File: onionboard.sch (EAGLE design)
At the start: 173 parts, among them IC1 IR4427S, IC2 IR4427S, J1 22-27-2041-04, Q1 FDD4141TO252, Q2 FDD4141TO252, Q3 FDD4141TO252, Q4 FDD4141TO252, Q5 FDD4141TO252, Q6 FDD4141TO252, X1 5569-8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

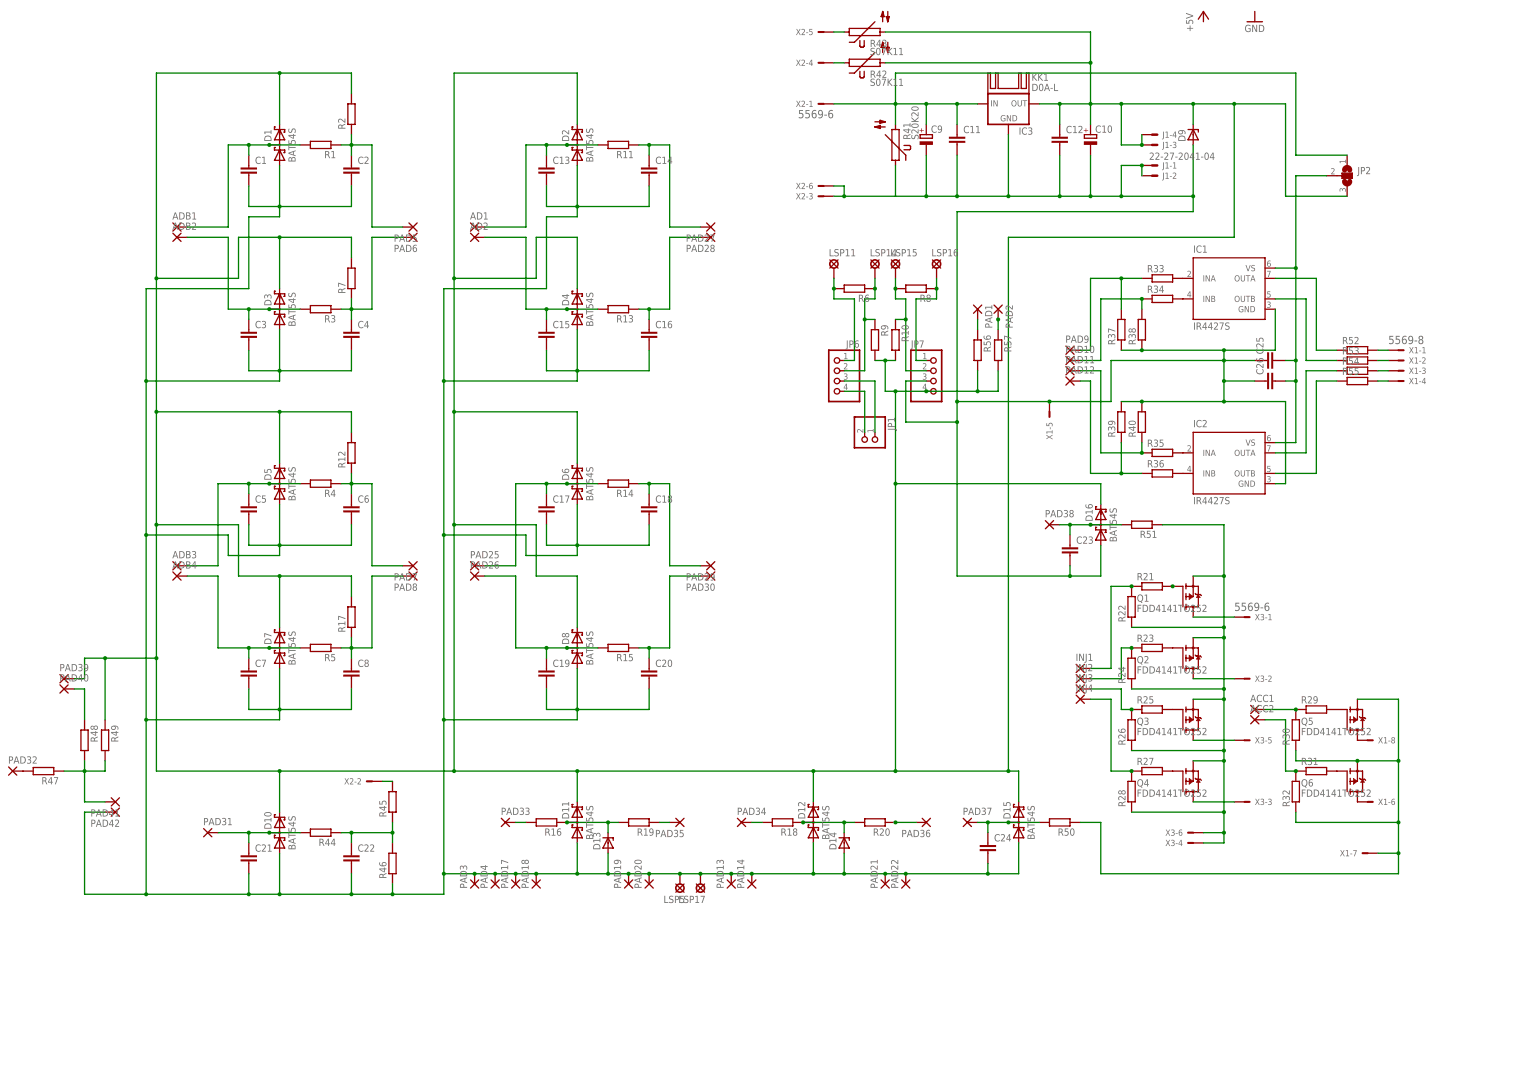
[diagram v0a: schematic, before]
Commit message: Cleaned up and rearranged the schematic. Moved two ground vias on monitor schottkys
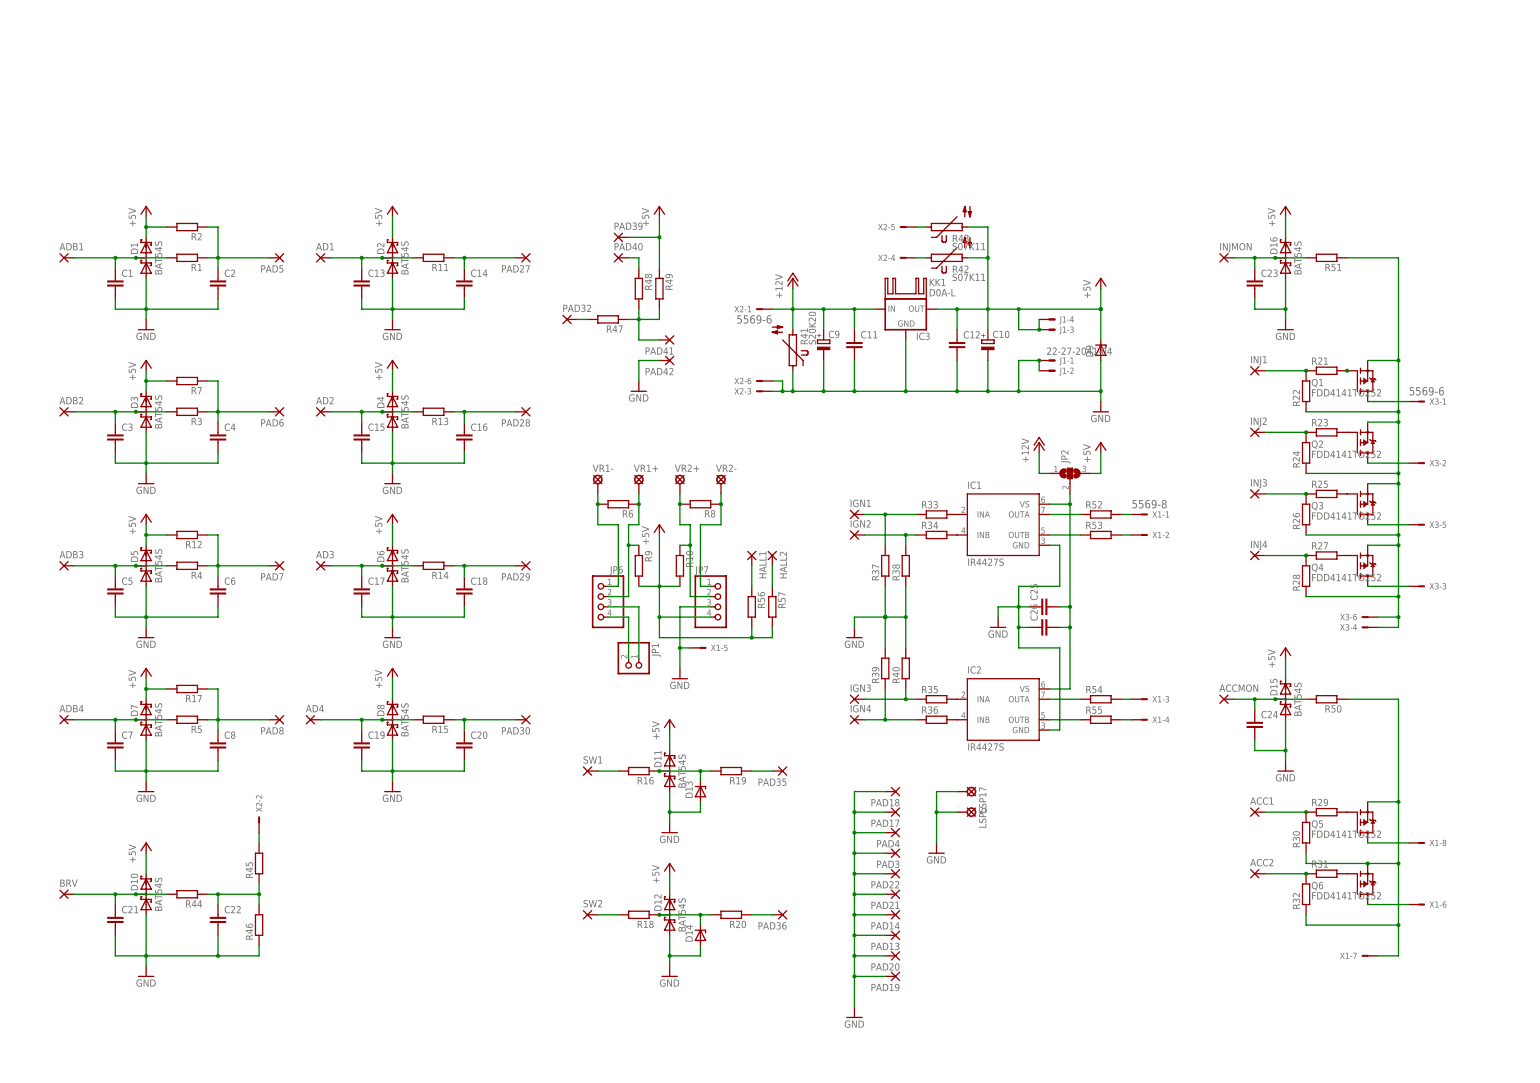
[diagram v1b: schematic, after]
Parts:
- removed LSP11, LSP14, LSP15, LSP16: LSP10, solpad:LSP10
- removed PAD1, PAD2: (no value), wirepad:1,6/0,8
- removed PAD10, PAD11, PAD12, PAD25, PAD26, PAD31, PAD33, PAD34, PAD37, PAD38, PAD9: (no value), wirepad:SMD2
- added ACCMON, AD3, AD4, BRV, IGN1, IGN2, IGN3, IGN4, INJMON, SW1, SW2: (no value), wirepad:SMD2
- added HALL1, HALL2: (no value), wirepad:1,6/0,8
- added VR1+, VR1-, VR2+, VR2-: LSP10, solpad:LSP10
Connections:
- net 12VOLT renamed +12V
- net 5VOLT renamed +5V
- net GND2 renamed GND
- net N$11: now also AD3.P; no longer PAD25.P
- net N$12: now also IGN1.P; no longer PAD9.P
- net N$13: now also AD4.P; no longer PAD26.P
- net N$14: now also IGN2.P; no longer PAD10.P
- net N$25: now also IGN3.P; no longer PAD11.P
- net N$26: now also IGN4.P; no longer PAD12.P
- net N$30: now also VR1-.MP; no longer LSP11.MP
- net N$33: now also VR1+.MP; no longer LSP14.MP
- net N$34: now also VR2+.MP; no longer LSP15.MP
- net N$35: now also VR2-.MP; no longer LSP16.MP
- net N$36: now also ACCMON.P; no longer PAD37.P
- net N$37: now also INJMON.P; no longer PAD38.P
- net N$67: now also BRV.P; no longer PAD31.P
- net N$70: now also HALL2.P; no longer PAD2.P
- net N$71: now also SW1.P; no longer PAD33.P
- net N$73: now also SW2.P; no longer PAD34.P
- net N$74: now also HALL1.P; no longer PAD1.P
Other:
- moved on the sheet: ACC1, ACC2, AD1, AD2, ADB1, ADB2, ADB3, ADB4, C1, C10, C11, C12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

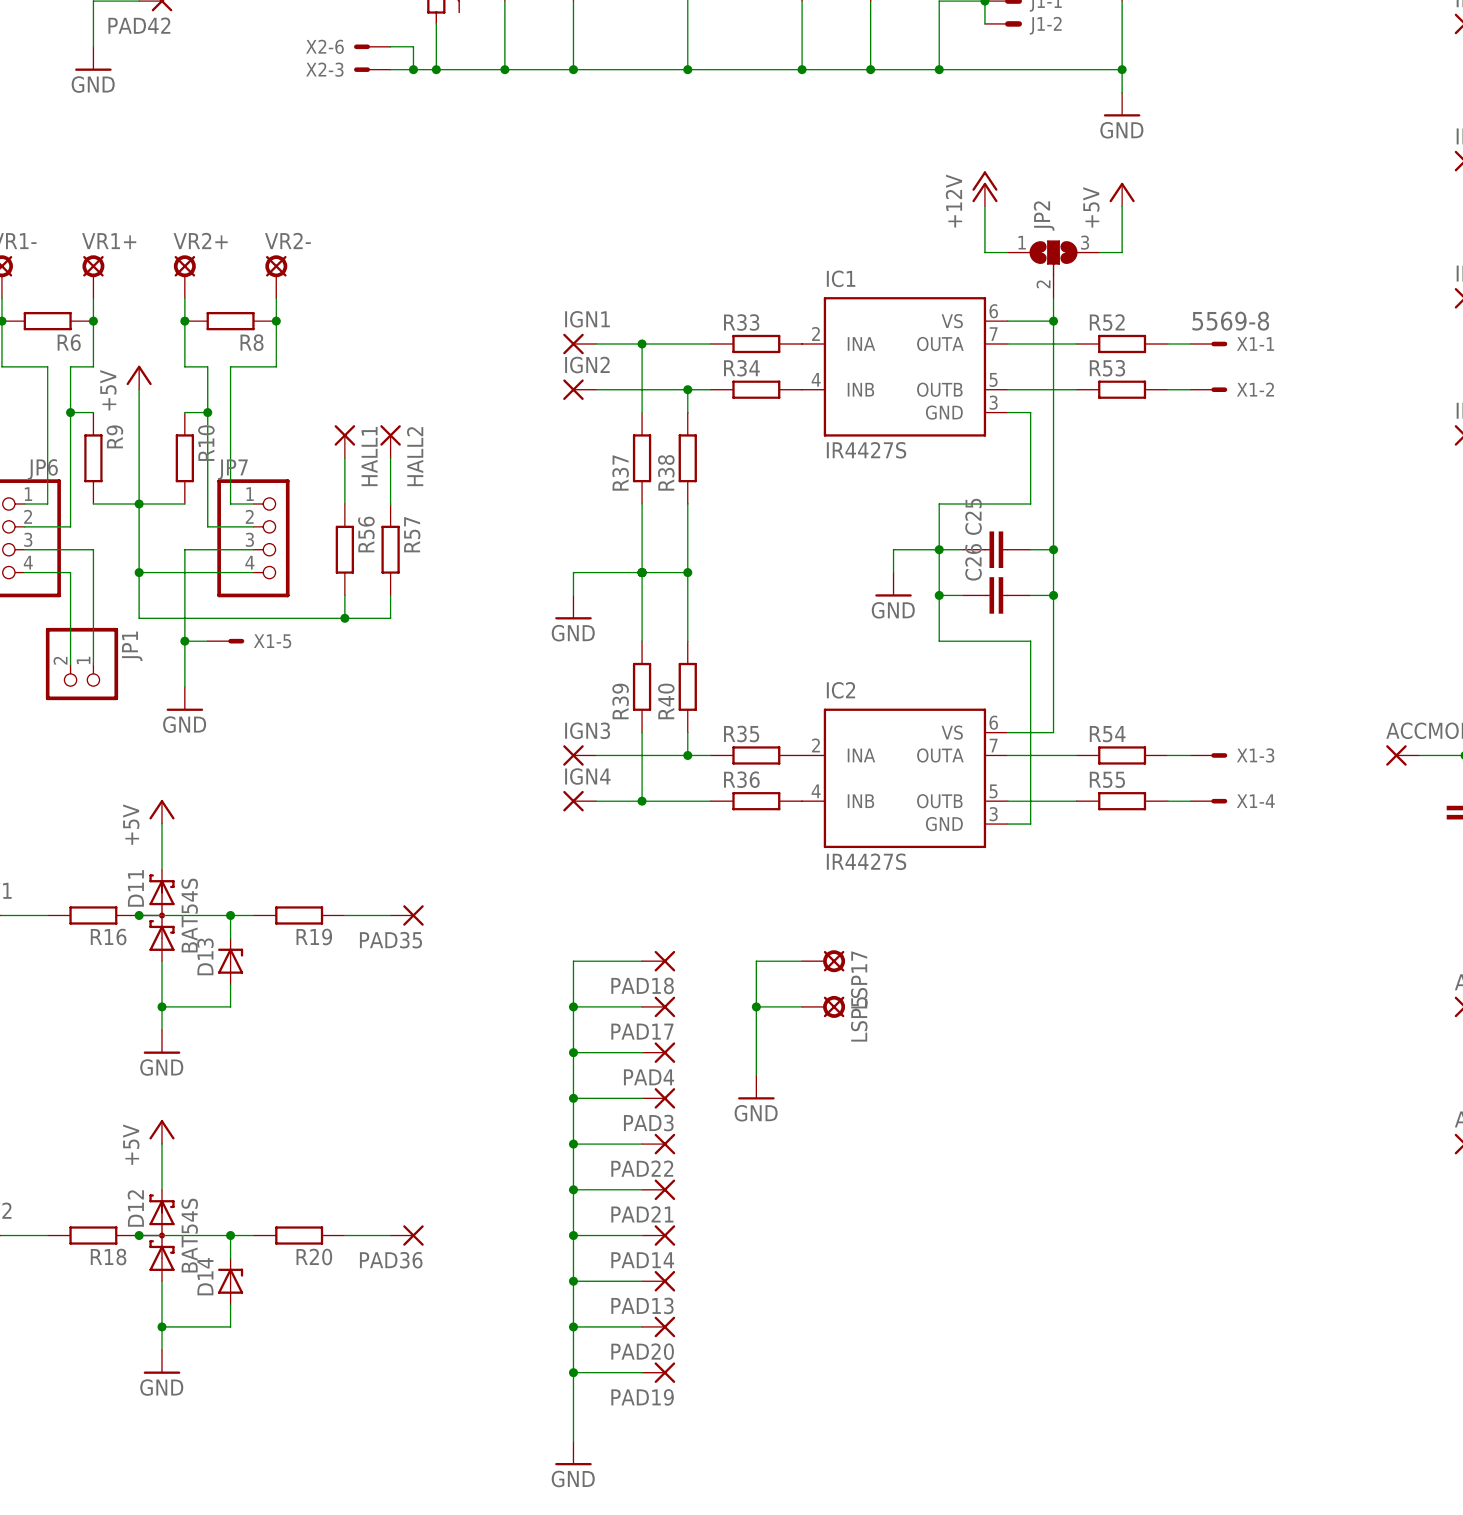
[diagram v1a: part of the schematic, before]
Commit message: more schematic clean up
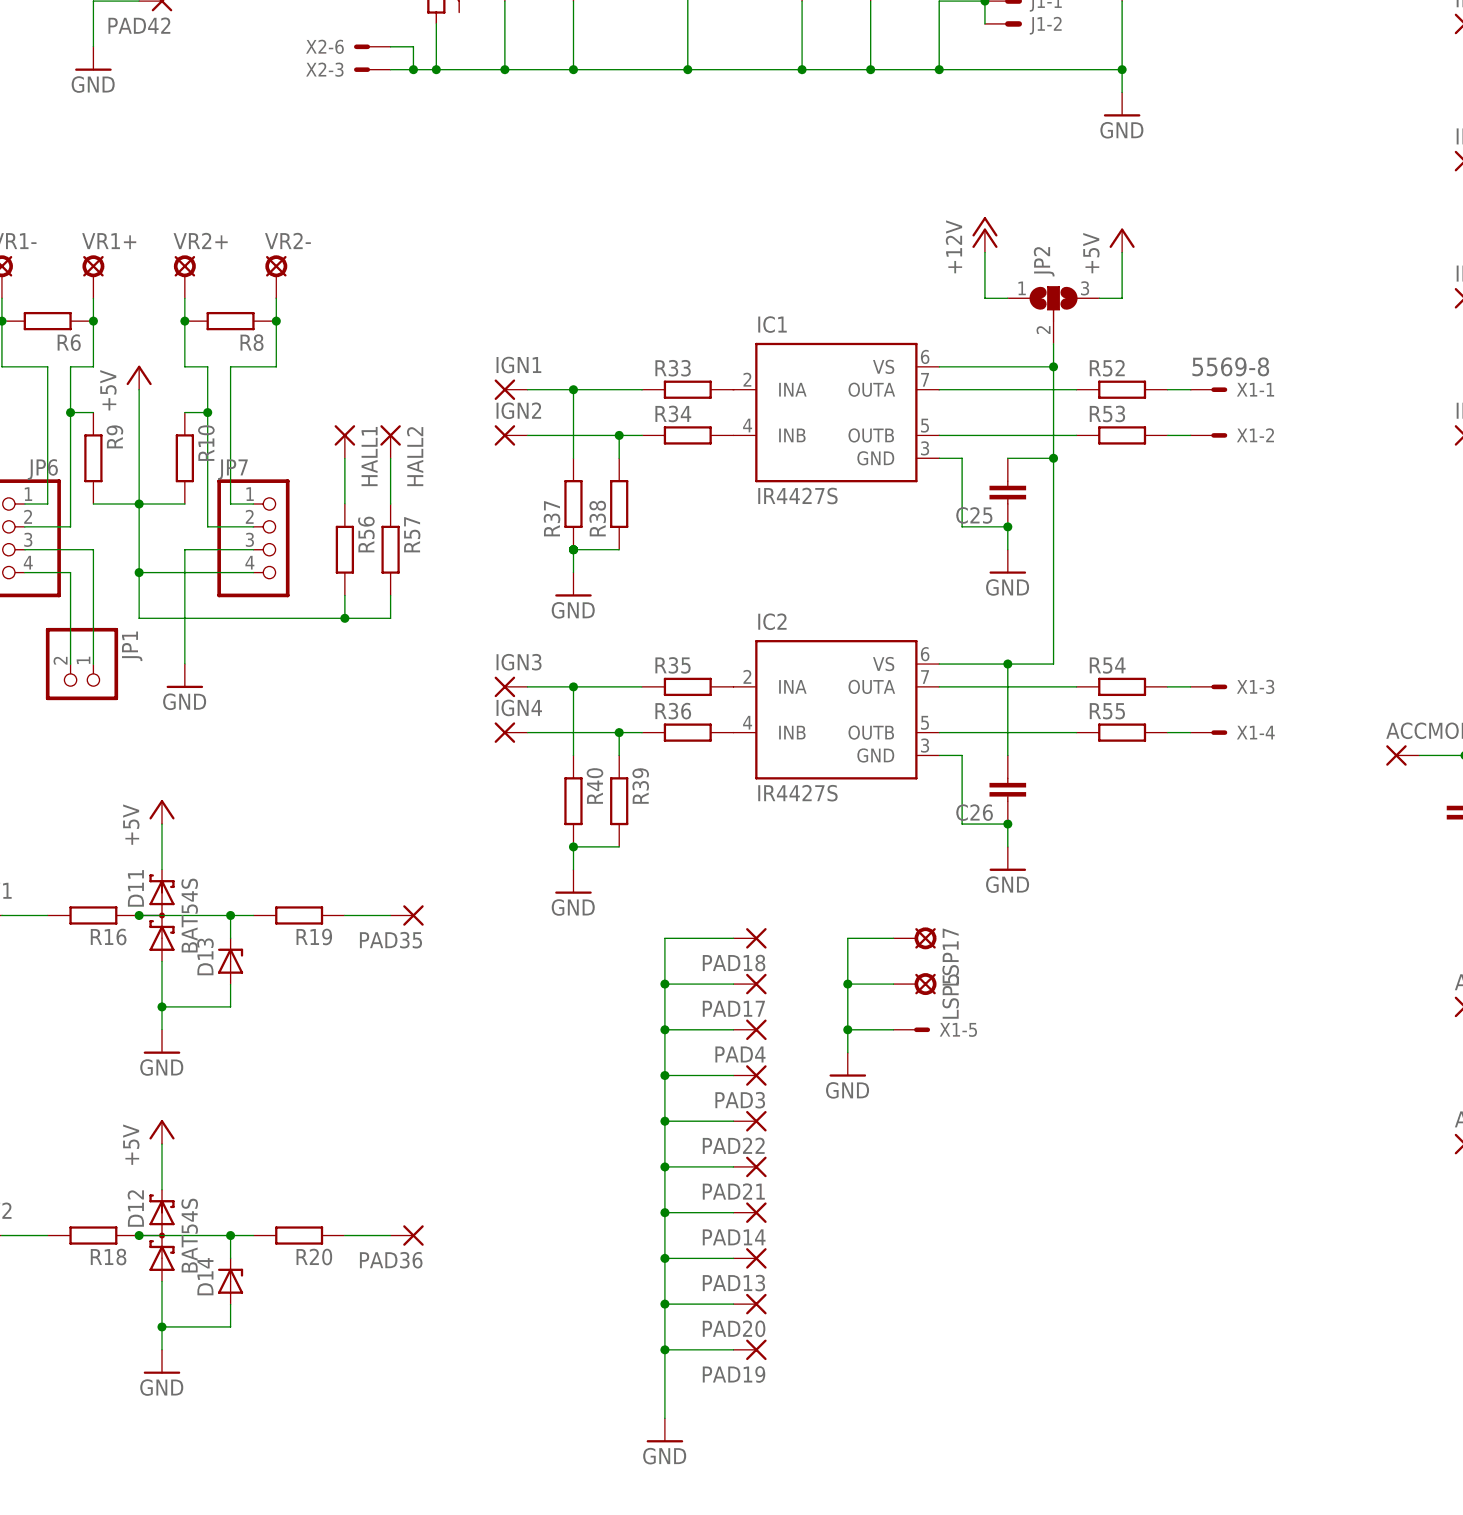
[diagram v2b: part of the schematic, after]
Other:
- moved on the sheet: C25, C26, IC1, IC2, IGN1, IGN2, IGN3, IGN4, JP2, LSP17, LSP5, PAD13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
